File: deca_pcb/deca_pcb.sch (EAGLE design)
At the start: 2 parts, among them IC1 DWM1000, U1 ATMEGA328P-PU

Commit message: updates
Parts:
- added Q1: (no value), crystal-geyer_V1_0:KX-9B
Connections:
- new net N$7: Q1.2, U1.PB6
- new net N$8: Q1.1, U1.PB7
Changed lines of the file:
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@@
 <part name="IC1" library="decawave" deviceset="DWM1000" device=""/>
 <part name="U1" library="atmel-element14" deviceset="ATMEGA328P-PU" device=""/>
+<part name="Q1" library="crystal-geyer_V1_0" library_urn="urn:adsk.eagle:library:203" deviceset="KX" device="-9B" package3d_urn="urn:adsk.eagle:package:11930/1"/>
 </parts>
 <sheets>
@@
 <attribute name="NAME" x="-5.5626" y="79.9338" size="2.0828" layer="95" ratio="10" rot="SR0"/>
 <attribute name="VALUE" x="-4.9784" y="27.3812" size="2.0828" layer="96" ratio="10" rot="SR0"/>
+</instance>
+<instance part="Q1" gate="G$1" x="-45.72" y="45.72" smashed="yes" rot="R90">
+<attribute name="NAME" x="-46.99" y="49.53" size="1.778" layer="95" rot="R90"/>
+<attribute name="VALUE" x="-43.18" y="49.53" size="1.778" layer="96" rot="R90"/>
 </instance>
 </instances>
@@
 </segment>
 </net>
+<net name="N$7" class="0">
+<segment>
+<pinref part="U1" gate="A" pin="PB6"/>
+<wire x1="-17.78" y1="45.72" x2="-35.56" y2="45.72" width="0.1524" layer="91"/>
+<wire x1="-35.56" y1="45.72" x2="-35.56" y2="48.26" width="0.1524" layer="91"/>
+<wire x1="-35.56" y1="48.26" x2="-45.72" y2="48.26" width="0.1524" layer="91"/>
+<pinref part="Q1" gate="G$1" pin="2"/>
+</segment>
+</net>
+<net name="N$8" class="0">
+<segment>
+<pinref part="U1" gate="A" pin="PB7"/>
+<wire x1="-45.72" y1="43.18" x2="-17.78" y2="43.18" width="0.1524" layer="91"/>
+<pinref part="Q1" gate="G$1" pin="1"/>
+</segment>
+</net>
 </nets>
 </sheet>
@@
 </schematic>
 </drawing>
+<compatibility>
+<note version="8.2" severity="warning">
+Since Version 8.2, EAGLE supports online libraries. The ids
+of those online libraries will not be understood (or retained)
+with this version.
+</note>
+<note version="8.3" severity="warning">
+Since Version 8.3, EAGLE supports URNs for individual library
+assets (packages, symbols, and devices). The URNs of those assets
+will not be understood (or retained) with this version.
+</note>
+<note version="8.3" severity="warning">
+Since Version 8.3, EAGLE supports the association of 3D packages
+with devices in libraries, schematics, and board files. Those 3D
+packages will not be understood (or retained) with this version.
+</note>
+</compatibility>
 </eagle>

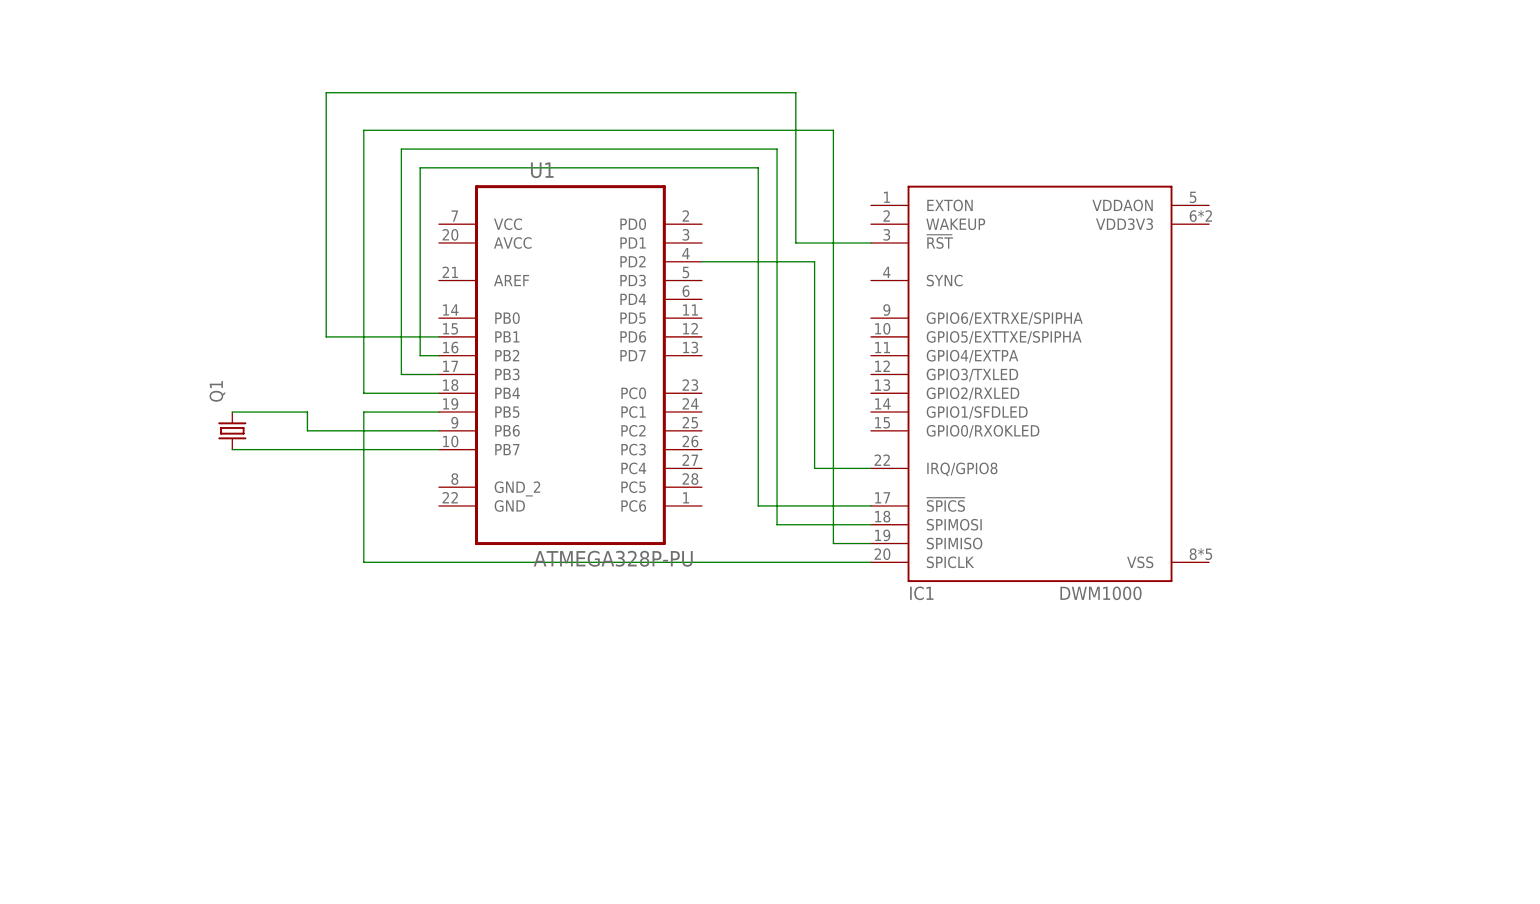
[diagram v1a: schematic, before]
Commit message: added components
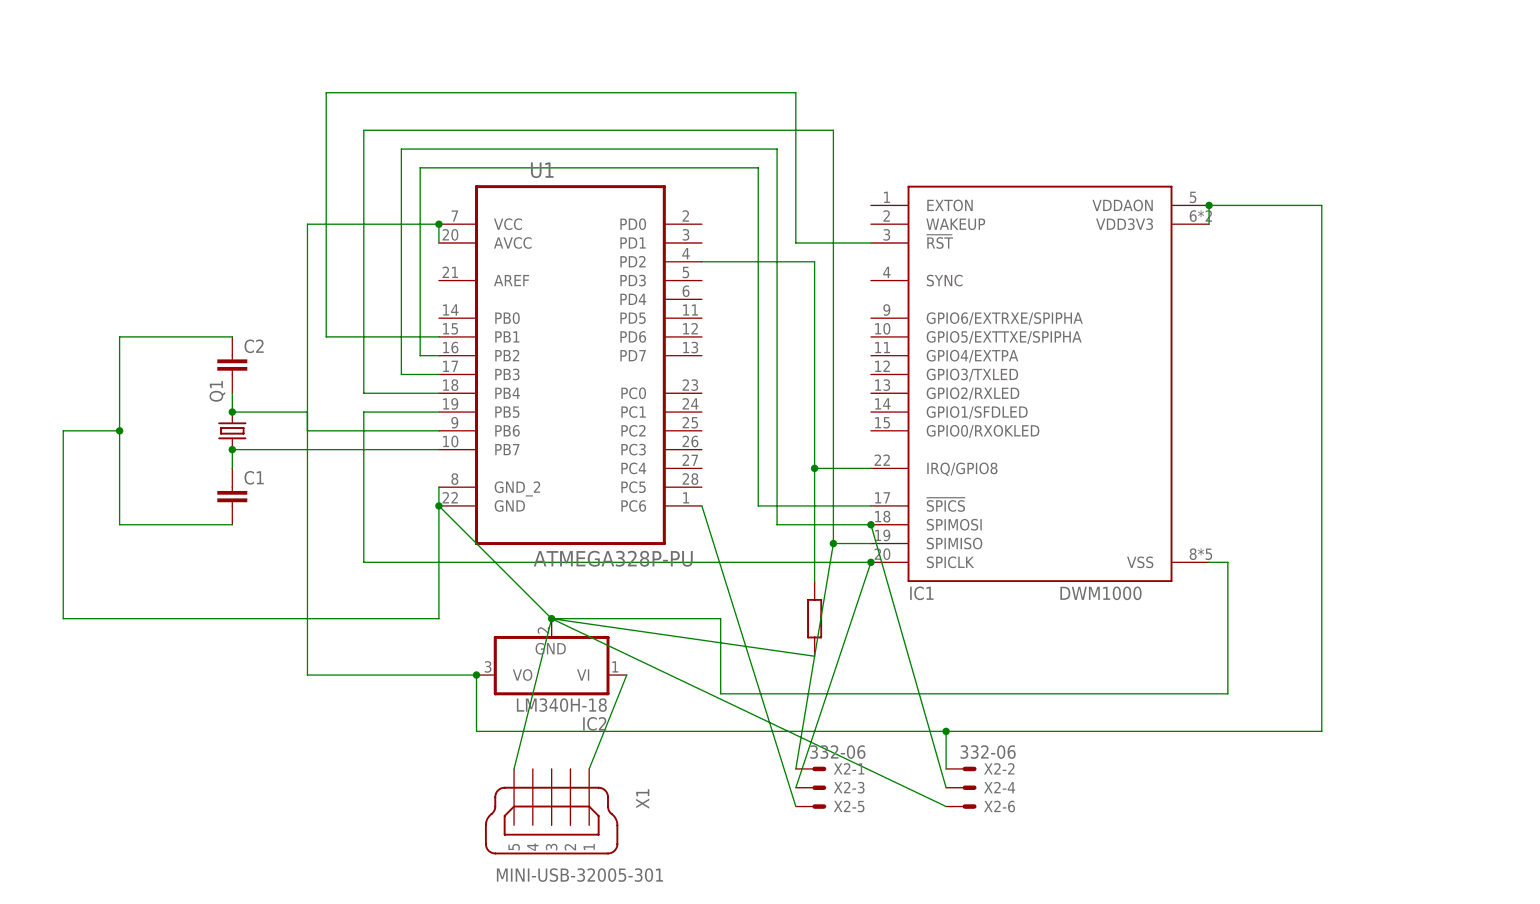
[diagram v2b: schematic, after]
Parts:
- added C1, C2: (no value), capacitor-wima:C2.5/6
- added IC2: LM340H-18, linear:LM340H-18
- added X1: MINI-USB-32005-301, con-cypressindustries:MINI-USB-32005-301
- added X2: 332-06, con-garry:332-06
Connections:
- new net N$10: IC2.VI, X1.1
- new net N$11: C1.2, C2.1, IC1.VSS, IC2.GND, U1.GND, U1.GND_2, X1.5, X2-6.S
- new net N$12: IC1.VDD3V3, IC1.VDDAON, IC2.VO, U1.AVCC, U1.VCC, X2-2.S
- new net N$9: U1.PC6, X2-5.S
- net N$1: now also X2-3.S
- net N$2: now also X2-1.S
- net N$3: now also X2-4.S
- net N$7: now also C2.2
- net N$8: now also C1.1
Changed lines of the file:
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@@
 <part name="U1" library="atmel-element14" deviceset="ATMEGA328P-PU" device=""/>
 <part name="Q1" library="crystal-geyer_V1_0" library_urn="urn:adsk.eagle:library:203" deviceset="KX" device="-9B" package3d_urn="urn:adsk.eagle:package:11930/1"/>
+<part name="C1" library="capacitor-wima" library_urn="urn:adsk.eagle:library:116" deviceset="C" device="2.5/6" package3d_urn="urn:adsk.eagle:package:5406/1"/>
+<part name="C2" library="capacitor-wima" library_urn="urn:adsk.eagle:library:116" deviceset="C" device="2.5/6" package3d_urn="urn:adsk.eagle:package:5406/1"/>
+<part name="X1" library="con-cypressindustries" library_urn="urn:adsk.eagle:library:138" deviceset="MINI-USB-" device="32005-301" package3d_urn="urn:adsk.eagle:package:6446/1"/>
+<part name="IC2" library="linear" library_urn="urn:adsk.eagle:library:262" deviceset="LM340?-*" device="H" package3d_urn="urn:adsk.eagle:package:16414/1" technology="18"/>
+<part name="R1" library="docu-dummy" library_urn="urn:adsk.eagle:library:215" deviceset="R" device=""/>
+<part name="X2" library="con-garry" library_urn="urn:adsk.eagle:library:147" deviceset="332-06" device="" package3d_urn="urn:adsk.eagle:package:6811/1"/>
 </parts>
 <sheets>
@@
 <attribute name="VALUE" x="-43.18" y="49.53" size="1.778" layer="96" rot="R90"/>
 </instance>
+<instance part="C1" gate="G$1" x="-45.72" y="38.1" smashed="yes">
+<attribute name="NAME" x="-44.196" y="38.481" size="1.778" layer="95"/>
+<attribute name="VALUE" x="-44.196" y="33.401" size="1.778" layer="96"/>
+</instance>
+<instance part="C2" gate="G$1" x="-45.72" y="55.88" smashed="yes">
+<attribute name="NAME" x="-44.196" y="56.261" size="1.778" layer="95"/>
+<attribute name="VALUE" x="-44.196" y="51.181" size="1.778" layer="96"/>
+</instance>
+<instance part="X1" gate="G$1" x="-2.54" y="-5.08" smashed="yes" rot="R270">
+<attribute name="NAME" x="8.89" y="-2.54" size="1.778" layer="95" rot="R270"/>
+<attribute name="VALUE" x="-10.16" y="-15.24" size="1.778" layer="96"/>
+</instance>
+<instance part="IC2" gate="A" x="-2.54" y="12.7" smashed="yes" rot="R180">
+<attribute name="NAME" x="5.08" y="6.985" size="1.778" layer="95" rot="R180"/>
+<attribute name="VALUE" x="5.08" y="9.525" size="1.778" layer="96" rot="R180"/>
+</instance>
+<instance part="R1" gate="G$1" x="33.02" y="20.32" smashed="yes" rot="R90"/>
+<instance part="X2" gate="-1" x="33.02" y="0" smashed="yes">
+<attribute name="NAME" x="35.56" y="-0.762" size="1.524" layer="95"/>
+<attribute name="VALUE" x="32.258" y="1.397" size="1.778" layer="96"/>
+</instance>
+<instance part="X2" gate="-2" x="53.34" y="0" smashed="yes">
+<attribute name="NAME" x="55.88" y="-0.762" size="1.524" layer="95"/>
+<attribute name="VALUE" x="52.578" y="1.397" size="1.778" layer="96"/>
+</instance>
+<instance part="X2" gate="-3" x="33.02" y="-2.54" smashed="yes">
+<attribute name="NAME" x="35.56" y="-3.302" size="1.524" layer="95"/>
+</instance>
+<instance part="X2" gate="-4" x="53.34" y="-2.54" smashed="yes">
+<attribute name="NAME" x="55.88" y="-3.302" size="1.524" layer="95"/>
+</instance>
+<instance part="X2" gate="-5" x="33.02" y="-5.08" smashed="yes">
+<attribute name="NAME" x="35.56" y="-5.842" size="1.524" layer="95"/>
+</instance>
+<instance part="X2" gate="-6" x="53.34" y="-5.08" smashed="yes">
+<attribute name="NAME" x="55.88" y="-5.842" size="1.524" layer="95"/>
+</instance>
 </instances>
 <busses>
@@
 <wire x1="-27.94" y1="48.26" x2="-27.94" y2="27.94" width="0.1524" layer="91"/>
 <wire x1="-27.94" y1="27.94" x2="40.64" y2="27.94" width="0.1524" layer="91"/>
+<pinref part="X2" gate="-3" pin="S"/>
+<wire x1="40.64" y1="27.94" x2="30.48" y2="-2.54" width="0.1524" layer="91"/>
+<junction x="40.64" y="27.94"/>
 </segment>
 </net>
@@
 <pinref part="IC1" gate="G$1" pin="SPIMISO"/>
 <wire x1="35.56" y1="30.48" x2="40.64" y2="30.48" width="0.1524" layer="91"/>
+<pinref part="X2" gate="-1" pin="S"/>
+<wire x1="35.56" y1="30.48" x2="30.48" y2="0" width="0.1524" layer="91"/>
+<junction x="35.56" y="30.48"/>
 </segment>
 </net>
@@
 <pinref part="IC1" gate="G$1" pin="SPIMOSI"/>
 <wire x1="27.94" y1="33.02" x2="40.64" y2="33.02" width="0.1524" layer="91"/>
+<pinref part="X2" gate="-4" pin="S"/>
+<wire x1="40.64" y1="33.02" x2="50.8" y2="-2.54" width="0.1524" layer="91"/>
+<junction x="40.64" y="33.02"/>
 </segment>
 </net>
@@
 <pinref part="IC1" gate="G$1" pin="IRQ/GPIO8"/>
 <wire x1="33.02" y1="40.64" x2="40.64" y2="40.64" width="0.1524" layer="91"/>
+<wire x1="33.02" y1="25.4" x2="33.02" y2="40.64" width="0.1524" layer="91"/>
+<junction x="33.02" y="40.64"/>
 </segment>
 </net>
@@
 <wire x1="-35.56" y1="48.26" x2="-45.72" y2="48.26" width="0.1524" layer="91"/>
 <pinref part="Q1" gate="G$1" pin="2"/>
+<pinref part="C2" gate="G$1" pin="2"/>
+<wire x1="-45.72" y1="50.8" x2="-45.72" y2="48.26" width="0.1524" layer="91"/>
+<junction x="-45.72" y="48.26"/>
 </segment>
 </net>
@@
 <wire x1="-45.72" y1="43.18" x2="-17.78" y2="43.18" width="0.1524" layer="91"/>
 <pinref part="Q1" gate="G$1" pin="1"/>
-</segment>
-</net>
+<pinref part="C1" gate="G$1" pin="1"/>
+<wire x1="-45.72" y1="43.18" x2="-45.72" y2="40.64" width="0.1524" layer="91"/>
+<junction x="-45.72" y="43.18"/>
+</segment>
+</net>
+<net name="N$10" class="0">
+<segment>
+<pinref part="X1" gate="G$1" pin="1"/>
+<pinref part="IC2" gate="A" pin="VI"/>
+<wire x1="2.54" y1="0" x2="7.62" y2="12.7" width="0.1524" layer="91"/>
+</segment>
+</net>
+<net name="N$11" class="0">
+<segment>
+<pinref part="X1" gate="G$1" pin="5"/>
+<pinref part="IC2" gate="A" pin="GND"/>
+<wire x1="-7.62" y1="0" x2="-2.54" y2="20.32" width="0.1524" layer="91"/>
+<pinref part="C1" gate="G$1" pin="2"/>
+<wire x1="-45.72" y1="33.02" x2="-60.96" y2="33.02" width="0.1524" layer="91"/>
+<wire x1="-60.96" y1="33.02" x2="-60.96" y2="45.72" width="0.1524" layer="91"/>
+<pinref part="C2" gate="G$1" pin="1"/>
+<wire x1="-60.96" y1="45.72" x2="-60.96" y2="58.42" width="0.1524" layer="91"/>
+<wire x1="-60.96" y1="58.42" x2="-45.72" y2="58.42" width="0.1524" layer="91"/>
+<wire x1="-60.96" y1="45.72" x2="-68.58" y2="45.72" width="0.1524" layer="91"/>
+<junction x="-60.96" y="45.72"/>
+<wire x1="-68.58" y1="45.72" x2="-68.58" y2="20.32" width="0.1524" layer="91"/>
+<wire x1="-68.58" y1="20.32" x2="-17.78" y2="20.32" width="0.1524" layer="91"/>
+<pinref part="U1" gate="A" pin="GND"/>
+<wire x1="-17.78" y1="20.32" x2="-17.78" y2="35.56" width="0.1524" layer="91"/>
+<wire x1="-2.54" y1="20.32" x2="-17.78" y2="35.56" width="0.1524" layer="91"/>
+<junction x="-2.54" y="20.32"/>
+<junction x="-17.78" y="35.56"/>
+<pinref part="U1" gate="A" pin="GND_2"/>
+<wire x1="-17.78" y1="35.56" x2="-17.78" y2="38.1" width="0.1524" layer="91"/>
+<wire x1="33.02" y1="15.24" x2="-2.54" y2="20.32" width="0.1524" layer="91"/>
+<wire x1="-2.54" y1="20.32" x2="20.32" y2="20.32" width="0.1524" layer="91"/>
+<wire x1="20.32" y1="20.32" x2="20.32" y2="10.16" width="0.1524" layer="91"/>
+<wire x1="20.32" y1="10.16" x2="88.9" y2="10.16" width="0.1524" layer="91"/>
+<wire x1="88.9" y1="10.16" x2="88.9" y2="27.94" width="0.1524" layer="91"/>
+<pinref part="IC1" gate="G$1" pin="VSS"/>
+<wire x1="88.9" y1="27.94" x2="86.36" y2="27.94" width="0.1524" layer="91"/>
+<pinref part="X2" gate="-6" pin="S"/>
+<wire x1="-2.54" y1="20.32" x2="50.8" y2="-5.08" width="0.1524" layer="91"/>
+</segment>
+</net>
+<net name="N$12" class="0">
+<segment>
+<pinref part="IC2" gate="A" pin="VO"/>
+<wire x1="-12.7" y1="12.7" x2="-35.56" y2="12.7" width="0.1524" layer="91"/>
+<wire x1="-35.56" y1="12.7" x2="-35.56" y2="73.66" width="0.1524" layer="91"/>
+<pinref part="U1" gate="A" pin="VCC"/>
+<wire x1="-35.56" y1="73.66" x2="-17.78" y2="73.66" width="0.1524" layer="91"/>
+<pinref part="U1" gate="A" pin="AVCC"/>
+<wire x1="-17.78" y1="73.66" x2="-17.78" y2="71.12" width="0.1524" layer="91"/>
+<junction x="-17.78" y="73.66"/>
+<wire x1="-12.7" y1="12.7" x2="-12.7" y2="5.08" width="0.1524" layer="91"/>
+<junction x="-12.7" y="12.7"/>
+<wire x1="-12.7" y1="5.08" x2="50.8" y2="5.08" width="0.1524" layer="91"/>
+<wire x1="50.8" y1="5.08" x2="101.6" y2="5.08" width="0.1524" layer="91"/>
+<wire x1="101.6" y1="5.08" x2="101.6" y2="76.2" width="0.1524" layer="91"/>
+<pinref part="IC1" gate="G$1" pin="VDDAON"/>
+<wire x1="101.6" y1="76.2" x2="86.36" y2="76.2" width="0.1524" layer="91"/>
+<pinref part="IC1" gate="G$1" pin="VDD3V3"/>
+<wire x1="86.36" y1="73.66" x2="86.36" y2="76.2" width="0.1524" layer="91"/>
+<junction x="86.36" y="76.2"/>
+<pinref part="X2" gate="-2" pin="S"/>
+<wire x1="50.8" y1="0" x2="50.8" y2="5.08" width="0.1524" layer="91"/>
+<junction x="50.8" y="5.08"/>
+</segment>
+</net>
+<net name="N$9" class="0">
+<segment>
+<pinref part="U1" gate="A" pin="PC6"/>
+<pinref part="X2" gate="-5" pin="S"/>
+<wire x1="17.78" y1="35.56" x2="30.48" y2="-5.08" width="0.1524" layer="91"/>
+</segment>
+</net>

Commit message: board pcb done
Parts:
- removed IC2: LM340H-18, linear:LM340H-18
- removed Q1: (no value), crystal-geyer_V1_0:KX-9B
- removed X2: 332-06, con-garry:332-06
- added C3: (no value), microbuilder:CAP_ELECTROLYTICPTH_3.5MMGRID_8MMDIA
- added IC3: (no value), lf33:LFXXCVS
- added JP1, JP2, JP3, JP4, JP7: (no value), jumper:JP1Q
- added JP10, JP12, JP13, JP14, JP15, JP5, JP6, JP8, JP9: (no value), con-pinhead:PINHD-1X1_2.54
- added TR1: (no value), discrete:THERMISTOR_R-5
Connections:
- new net N$13: C1.2, C2.1, IC1.VSS, IC3.GND, JP6.1, TR1.2, U1.GND, U1.GND_2, X1.5
- new net N$14: IC1.SPIMISO, JP2.1
- new net N$15: IC1.SPIMOSI, JP3.1
- new net N$16: IC1.!SPICS, JP4.1
- new net N$17: JP8.1, U1.PD0
- new net N$18: JP9.1, U1.PD1
- new net N$19: JP12.1, U1.PC6
- net N$1: now also JP1.2, JP15.1; no longer IC1.SPICLK, X2-3.S
- net N$10: now also IC3.IN, JP5.1; no longer IC2.VI
- net N$11: now also IC1.SPICLK, JP1.1; no longer C1.2, C2.1, IC1.VSS, IC2.GND, U1.GND, U1.GND_2, X1.5, X2-6.S
- net N$12: now also IC3.OUT, JP10.1, JP7.1; no longer IC1.VDD3V3, IC1.VDDAON, IC2.VO, X2-2.S
- net N$2: now also JP14.1, JP2.2; no longer IC1.SPIMISO, X2-1.S
- net N$3: now also JP13.1, JP3.2; no longer IC1.SPIMOSI, X2-4.S
- net N$4: now also JP4.2; no longer IC1.!SPICS
- net N$5: now also TR1.1
- net N$7: now also C3.+; no longer Q1.2
- net N$8: now also C3.-; no longer Q1.1
- net N$9: now also IC1.VDD3V3, IC1.VDDAON, JP7.2; no longer U1.PC6, X2-5.S
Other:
- moved on the sheet: IC1

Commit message: txt
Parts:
- removed C3: (no value), microbuilder:CAP_ELECTROLYTICPTH_3.5MMGRID_8MMDIA
- added Q1: (no value), crystal:CRYSTALHC49S
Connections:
- net N$12 renamed VCC
- net N$17 renamed JP8
- removed net N$13: C1.2, C2.1, IC1.VSS, IC3.GND, JP6.1, TR1.2, U1.GND, U1.GND_2, X1.5
- new net GND: C1.2, C2.2, IC1.VSS, IC3.GND, JP6.1, TR1.2, U1.GND, U1.GND_2, X1.5
- net N$7: now also C2.1, Q1.1; no longer C2.2, C3.+
- net N$8: now also Q1.2; no longer C3.-
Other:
- moved on the sheet: C1, C2, JP10, JP7, JP8
